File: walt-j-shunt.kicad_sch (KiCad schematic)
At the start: 39 parts, among them Q1 NMOS, Q2 PNP, Q3 PNP, U1 ${SIM.PARAMS}

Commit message: footprint placeholders
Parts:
- C4: footprint (none) -> Capacitor_THT:CP_Radial_D5.0mm_P2.00mm
- D5: footprint (none) -> Diode_SMD:D_0805_2012Metric
- D6, D7: footprint (none) -> Diode_SMD:D_SMC
- D8, D9: footprint (none) -> Package_TO_SOT_SMD:SOT-23-3
- Q1: footprint (none) -> Package_TO_SOT_THT:TO-3P-3_Horizontal_TabDown
- U1: footprint (none) -> Package_SO:SOIC-8-1EP_3.9x4.9mm_P1.27mm_EP2.41x3.3mm
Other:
- moved on the sheet: D8, R11, R12
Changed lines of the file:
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@@
 	)
 	(junction
-		(at 213.36 93.98)
+		(at 226.06 86.36)
 		(diameter 0)
 		(color 0 0 0 0)
 	)
 	(junction
-		(at 226.06 86.36)
+		(at 127 86.36)
 		(diameter 0)
 		(color 0 0 0 0)
 	)
 	(junction
-		(at 127 86.36)
+		(at 213.36 95.25)
 		(diameter 0)
 		(color 0 0 0 0)
@@
 	(wire
 		(pts
-			(xy 213.36 93.98) (xy 213.36 95.25)
-		)
-		(stroke
-			(width 0)
-			(type default)
-		)
-	)
-	(wire
-		(pts
-			(xy 219.71 93.98) (xy 220.98 93.98)
+			(xy 219.71 95.25) (xy 220.98 95.25)
 		)
 		(stroke
@@
 	(wire
 		(pts
-			(xy 220.98 93.98) (xy 220.98 86.36)
+			(xy 220.98 95.25) (xy 220.98 86.36)
 		)
 		(stroke
@@
 	(wire
 		(pts
-			(xy 213.36 92.71) (xy 213.36 93.98)
-		)
-		(stroke
-			(width 0)
-			(type default)
-		)
-	)
-	(wire
-		(pts
 			(xy 180.34 106.68) (xy 181.61 106.68)
 		)
@@
 	(wire
 		(pts
-			(xy 207.01 93.98) (xy 207.01 99.06)
+			(xy 207.01 95.25) (xy 207.01 99.06)
 		)
 		(stroke
@@
 	(wire
 		(pts
-			(xy 213.36 93.98) (xy 214.63 93.98)
+			(xy 213.36 95.25) (xy 214.63 95.25)
 		)
 		(stroke
@@
 	(wire
 		(pts
-			(xy 213.36 102.87) (xy 213.36 105.41)
+			(xy 213.36 95.25) (xy 213.36 93.98)
+		)
+		(stroke
+			(width 0)
+			(type default)
+		)
+	)
+	(wire
+		(pts
+			(xy 213.36 104.14) (xy 213.36 105.41)
 		)
 		(stroke
@@
 	(wire
 		(pts
+			(xy 213.36 95.25) (xy 213.36 96.52)
+		)
+		(stroke
+			(width 0)
+			(type default)
+		)
+	)
+	(wire
+		(pts
 			(xy 83.82 86.36) (xy 88.9 86.36)
 		)
@@
 	(wire
 		(pts
-			(xy 212.09 93.98) (xy 213.36 93.98)
+			(xy 212.09 95.25) (xy 213.36 95.25)
 		)
 		(stroke
@@
 	(global_label "vref"
 		(shape input)
-		(at 213.36 92.71 90)
+		(at 213.36 93.98 90)
 		(fields_autoplaced yes)
 		(effects
@@
 		)
 		(property "Intersheetrefs" "${INTERSHEET_REFS}"
-			(at 213.36 86.1567 90)
+			(at 213.36 87.4267 90)
 			(effects
 				(font
@@
 	(symbol
 		(lib_id "Device:R_Small")
-		(at 209.55 93.98 270)
+		(at 209.55 95.25 270)
 		(unit 1)
 		(exclude_from_sim no)
@@
 		(fields_autoplaced yes)
 		(property "Reference" "R11"
-			(at 209.55 88.9 90)
+			(at 209.55 90.17 90)
 			(effects
 				(font
@@
 		)
 		(property "Value" "1k"
-			(at 209.55 91.44 90)
+			(at 209.55 92.71 90)
 			(effects
 				(font
@@
 		)
 		(property "Footprint" "Resistor_SMD:R_1206_3216Metric"
-			(at 209.55 93.98 0)
+			(at 209.55 95.25 0)
 			(effects
 				(font
@@
 		)
 		(property "Datasheet" "~"
-			(at 209.55 93.98 0)
+			(at 209.55 95.25 0)
 			(effects
 				(font
@@
 		)
 		(property "Description" "Resistor, small symbol"
-			(at 209.55 93.98 0)
+			(at 209.55 95.25 0)
 			(effects
 				(font
@@
 			)
 		)
-		(property "Footprint" ""
+		(property "Footprint" "Diode_SMD:D_SMC"
 			(at 194.31 102.87 0)
 			(effects
@@
 			)
 		)
-		(property "Footprint" ""
+		(property "Footprint" "Diode_SMD:D_SMC"
 			(at 187.96 102.87 0)
 			(effects
@@
 			)
 		)
-		(property "Footprint" ""
+		(property "Footprint" "Diode_SMD:D_0805_2012Metric"
 			(at 153.67 101.6 0)
 			(effects
@@
 			)
 		)
-		(property "Footprint" ""
+		(property "Footprint" "Package_TO_SOT_THT:TO-3P-3_Horizontal_TabDown"
 			(at 111.76 83.82 0)
 			(effects
@@
 			)
 		)
-		(property "Footprint" ""
+		(property "Footprint" "Package_TO_SOT_SMD:SOT-23-3"
 			(at 213.36 109.22 0)
 			(effects
@@
 	(symbol
 		(lib_id "Device:D_Zener")
-		(at 213.36 99.06 90)
+		(at 213.36 100.33 90)
 		(unit 1)
 		(exclude_from_sim no)
@@
 		(fields_autoplaced yes)
 		(property "Reference" "D8"
-			(at 215.9 97.7899 90)
+			(at 215.9 99.0599 90)
 			(effects
 				(font
@@
 		)
 		(property "Value" "D_Zener"
-			(at 215.9 100.3299 90)
+			(at 215.9 101.5999 90)
 			(effects
 				(font
@@
 			)
 		)
-		(property "Footprint" ""
-			(at 213.36 99.06 0)
+		(property "Footprint" "Package_TO_SOT_SMD:SOT-23-3"
+			(at 213.36 100.33 0)
 			(effects
 				(font
@@
 		)
 		(property "Datasheet" "~"
-			(at 213.36 99.06 0)
+			(at 213.36 100.33 0)
 			(effects
 				(font
@@
 		)
 		(property "Description" "Zener diode"
-			(at 213.36 99.06 0)
+			(at 213.36 100.33 0)
 			(effects
 				(font
@@
 		)
 		(property "Sim.Library" "/Users/cibo/Documents/spice/d.lib"
-			(at 213.36 99.06 0)
+			(at 213.36 100.33 0)
 			(effects
 				(font
@@
 		)
 		(property "Sim.Name" "BZX84C6V2L"
-			(at 213.36 99.06 0)
+			(at 213.36 100.33 0)
 			(effects
 				(font
@@
 		)
 		(property "Sim.Device" "D"
-			(at 213.36 99.06 0)
+			(at 213.36 100.33 0)
 			(effects
 				(font
@@
 		)
 		(property "Sim.Pins" "1=K 2=A"
-			(at 213.36 99.06 0)
+			(at 213.36 100.33 0)
 			(effects
 				(font
@@
 			)
 		)
-		(property "Footprint" ""
+		(property "Footprint" "Capacitor_THT:CP_Radial_D5.0mm_P2.00mm"
 			(at 161.29 110.49 0)
 			(effects
@@
 	(symbol
 		(lib_id "Device:R_Small")
-		(at 217.17 93.98 270)
+		(at 217.17 95.25 270)
 		(unit 1)
 		(exclude_from_sim no)
@@
 		(fields_autoplaced yes)
 		(property "Reference" "R12"
-			(at 217.17 88.9 90)
+			(at 217.17 90.17 90)
 			(effects
 				(font
@@
 		)
 		(property "Value" "1.82k"
-			(at 217.17 91.44 90)
+			(at 217.17 92.71 90)
 			(effects
 				(font
@@
 		)
 		(property "Footprint" "Resistor_SMD:R_1206_3216Metric"
-			(at 217.17 93.98 0)
+			(at 217.17 95.25 0)
 			(effects
 				(font
@@
 		)
 		(property "Datasheet" "~"
-			(at 217.17 93.98 0)
+			(at 217.17 95.25 0)
 			(effects
 				(font
@@
 		)
 		(property "Description" "Resistor, small symbol"
-			(at 217.17 93.98 0)
+			(at 217.17 95.25 0)
 			(effects
 				(font
@@
 			)
 		)
-		(property "Footprint" ""
+		(property "Footprint" "Package_SO:SOIC-8-1EP_3.9x4.9mm_P1.27mm_EP2.41x3.3mm"
 			(at 166.37 101.6 0)
 			(effects

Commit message: basic layout positive
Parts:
- removed U1: ${SIM.PARAMS}, Package_SO:SOIC-8-1EP_3.9x4.9mm_P1.27mm_EP2.41x3.3mm, symbol Simulation_SPICE:OPAMP
- removed V1: VSIN, Samacsys:395443002, symbol Simulation_SPICE:VSIN
- added U1: AD817, Package_SO:SOIC-8_3.9x4.9mm_P1.27mm, symbol Amplifier_Operational:AD817
- added V1: VPULSE, Samacsys:395443002, symbol Simulation_SPICE:VPULSE
- C1, C2: footprint Capacitor_THT:CP_Radial_D18.0mm_P7.50mm -> Capacitor_THT:CP_Radial_D12.5mm_P5.00mm
- C3: footprint Capacitor_THT:CP_Radial_D18.0mm_P7.50mm -> Samacsys:B32529C105J
- C4: footprint Capacitor_THT:CP_Radial_D5.0mm_P2.00mm -> Capacitor_SMD:C_0805_2012Metric
- D1, D2, D3, D4: footprint Diode_SMD:D_SMC -> Diode_SMD:D_SOD-123
- D6, D7: footprint Diode_SMD:D_SMC -> Diode_SMD:D_SOD-123F
- Q1: footprint Package_TO_SOT_THT:TO-3P-3_Horizontal_TabDown -> Package_TO_SOT_THT:TO-220-3_Horizontal_TabDown
- Q2: footprint Package_TO_SOT_THT:TO-3P-3_Horizontal_TabDown -> Package_TO_SOT_SMD:TO-252-2
- Q3: footprint Package_TO_SOT_THT:TO-3P-3_Horizontal_TabDown -> Package_TO_SOT_SMD:SOT-23-3
- R10, R9: footprint Resistor_SMD:R_1206_3216Metric -> Resistor_SMD:R_MELF_MMB-0207
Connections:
- net GND: now also U1.4 (V-)
- net ac: now also V1.1
- net out: now also U1.7 (V+)
- net pre-cur: now reaches C3.1, Q1.1 (D), R2.1
- net at D1.2 (A), D2.1 (K): now also V1.2
- net at C6.1, D6.2 (A), D7.1 (K)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: now also U1.3 (+)
- net at C4.2, D5.1 (K): now also U1.6
- net at C4.1, R8.2: now also U1.2 (-)
- no-connect marks 0 -> 2
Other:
- moved on the sheet: D1, D3

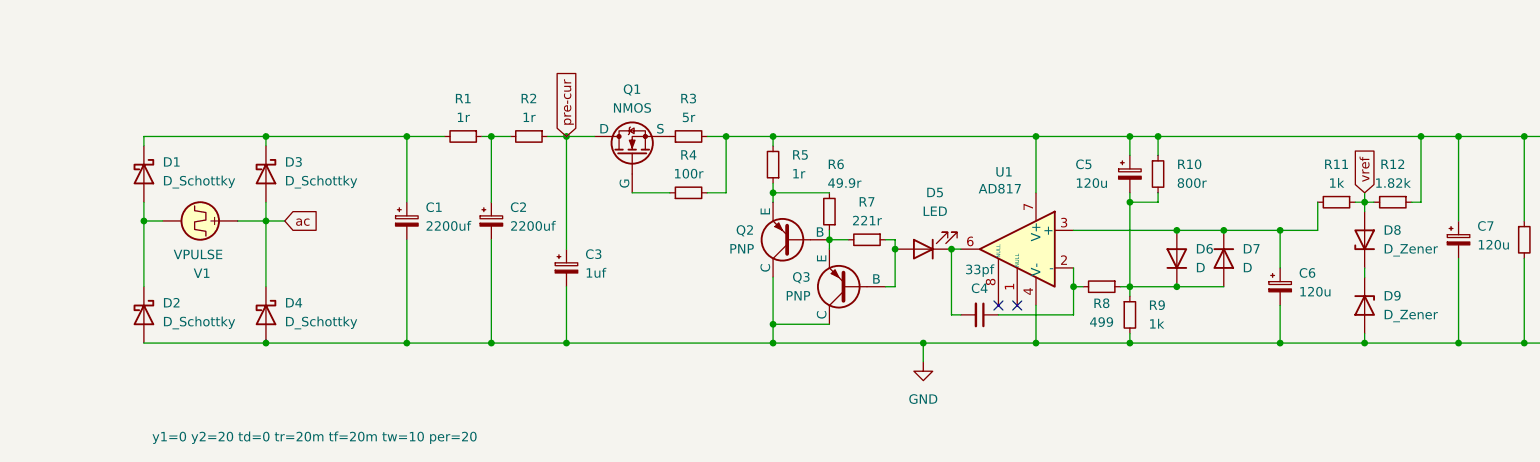
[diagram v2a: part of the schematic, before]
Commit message: plus only, cap and rectififer on board
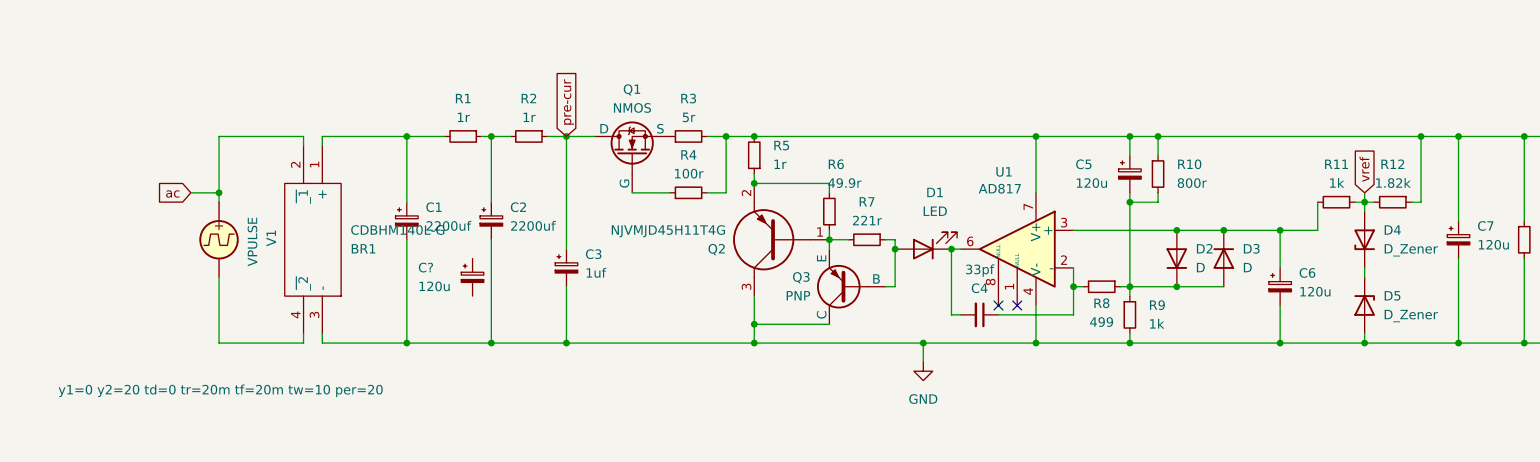
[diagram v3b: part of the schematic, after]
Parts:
- removed D1, D2, D3, D4: D_Schottky, Diode_SMD:D_SOD-123, symbol Device:D_Schottky
- removed Q2: PNP, Package_TO_SOT_SMD:TO-252-2, symbol Simulation_SPICE:PNP
- added BR1: CDBHM140L-G, Samacsys:CDBHM140LG, symbol Samacsys:CDBHM140L-G
- added C?: 120u, Capacitor_THT:CP_Radial_D5.0mm_P2.00mm, symbol Device:C_Polarized_Small
- added Q2: NJVMJD45H11T4G, Samacsys:DPAK_(SINGLE-GAUGE)_TO-252(369C)_ISSUE_F, symbol Samacsys:NJVMJD45H11T4G
- R13: footprint Resistor_SMD:R_2512_6332Metric -> Resistor_SMD:R_1206_3216Metric
- renumbered D5 to D1, D6 to D2, D7 to D3, D8 to D4, D9 to D5
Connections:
- net GND: now also BR1.3 (-), Q2.3
- net ac: now also BR1.2 (~{_1})
- net at Q3.3 (E), R6.1, R7.2: now also Q2.1
- net at R5.1, R6.2: now also Q2.2
- net at V1.2: now also BR1.4 (~{_2})
- net at C1.1, R1.2: now also BR1.1 (+)
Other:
- moved on the sheet: R5, V1

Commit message: working in subsheet
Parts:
- removed BR1: CDBHM140L-G, Samacsys:CDBHM140LG, symbol Samacsys:CDBHM140L-G
- removed C1, C2: 2200uf, Capacitor_THT:CP_Radial_D12.5mm_P5.00mm, symbol Device:C_Polarized_Small
- removed R1: 1r, Resistor_SMD:R_1206_3216Metric, symbol Device:R_Small
- removed R13: 1k, Resistor_SMD:R_1206_3216Metric, symbol Device:R_Small
- removed V1: VPULSE, Samacsys:395443002, symbol Simulation_SPICE:VPULSE
- added V1: VSIN, Samacsys:395443002, symbol Simulation_SPICE:VSIN
- D4, D5: footprint Package_TO_SOT_SMD:SOT-23-3 -> Diode_SMD:D_MiniMELF
- gave numbers to parts that had none: 1
- renumbered C3 to C2, C4 to C3, C5 to C4, C6 to C5, C7 to C6, R2 to R1, R11 to R10, R12 to R11, R3 to R2, R4 to R3, R5 to R4, R6 to R5, R7 to R6, R8 to R7, R9 to R8, R10 to R9
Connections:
- net GND: now also C1.2, V1.2
- net bank-plus: now reaches R1.2
- net bank-plus: now also C1.1, V1.1
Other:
- added sheet reg (reg.kicad_sch)
- moved on the sheet: C1, C2, I1, R1

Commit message: bipolar. untested
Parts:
- removed C3: 33pf, Capacitor_SMD:C_0805_2012Metric, symbol Device:C_Small
- removed C4, C5, C6: 120u, Capacitor_THT:CP_Radial_D5.0mm_P2.00mm, symbol Device:C_Polarized_Small
- removed D1: LED, Diode_SMD:D_0805_2012Metric, symbol Device:LED
- removed D2, D3: D, Diode_SMD:D_SOD-123F, symbol Device:D
- removed D4, D5: D_Zener, Diode_SMD:D_MiniMELF, symbol Device:D_Zener
- removed Q1: NMOS, Package_TO_SOT_THT:TO-220-3_Horizontal_TabDown, symbol Simulation_SPICE:NMOS
- removed Q2: NJVMJD45H11T4G, Samacsys:DPAK_(SINGLE-GAUGE)_TO-252(369C)_ISSUE_F, symbol Samacsys:NJVMJD45H11T4G
- removed Q3: PNP, Package_TO_SOT_SMD:SOT-23-3, symbol Simulation_SPICE:PNP
- removed R10: 1k, Resistor_SMD:R_1206_3216Metric, symbol Device:R_Small
- removed R11: 1.82k, Resistor_SMD:R_1206_3216Metric, symbol Device:R_Small
- removed R2: 5r, Resistor_SMD:R_1206_3216Metric, symbol Device:R_Small
- removed R3: 100r, Resistor_SMD:R_1206_3216Metric, symbol Device:R_Small
- removed R4: 1r, Resistor_SMD:R_1206_3216Metric, symbol Device:R_Small
- removed R5: 49.9r, Resistor_SMD:R_1206_3216Metric, symbol Device:R_Small
- removed R6: 221r, Resistor_SMD:R_1206_3216Metric, symbol Device:R_Small
- removed R7: 499, Resistor_SMD:R_1206_3216Metric, symbol Device:R_Small
- removed R8: 1k, Resistor_SMD:R_MELF_MMB-0207, symbol Device:R_Small
- removed R9: 800r, Resistor_SMD:R_MELF_MMB-0207, symbol Device:R_Small
- removed U1: AD817, Package_SO:SOIC-8_3.9x4.9mm_P1.27mm, symbol Amplifier_Operational:AD817
- added C7: 120u, Capacitor_THT:CP_Radial_D5.0mm_P2.00mm, symbol Device:C_Polarized_Small
- added C8: 1uf, Samacsys:B32529C105J, symbol Device:C_Polarized_Small
- added I2: 20ma, Samacsys:395443002, symbol Simulation_SPICE:IDC
- added R12: 1r, Resistor_SMD:R_1206_3216Metric, symbol Device:R_Small
- added V2: VSIN, Samacsys:395443002, symbol Simulation_SPICE:VSIN
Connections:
- net GND: now also C7.1, C8.1, I2.1, V2.1
- net out renamed pos_reg_out
- new net: C7.2, R12.2, V2.2
- new net current_source1/plus: C8.2, R12.1
- new net neg_reg_out: I2.2
- no-connect marks 2 -> 0
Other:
- added sheet current_source (current_source.kicad_sch)
- added sheet current_source1 (current_source.kicad_sch)
- added sheet reg1 (reg.kicad_sch)
- sheet reg ports: added minus, plus; removed none
- moved on the sheet: C1, I1, R1

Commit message: pretty neat neg needs testing
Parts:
- added J1: Screw_Terminal_01x03, TerminalBlock_Altech:Altech_AK100_1x03_P5.00mm, symbol Connector:Screw_Terminal_01x03
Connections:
- net GND: now also J1.2 (Pin_2)
- net neg_reg_out: now also J1.3 (Pin_3)
- net pos_reg_out: now also J1.1 (Pin_1)
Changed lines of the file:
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@@
 	(paper "A4")
 	(junction
+		(at 170.18 153.67)
+		(diameter 0)
+		(color 0 0 0 0)
+	)
+	(junction
 		(at 158.75 95.25)
 		(diameter 0)
@@
 	)
 	(junction
+		(at 170.18 95.25)
+		(diameter 0)
+		(color 0 0 0 0)
+	)
+	(junction
 		(at 97.79 114.3)
 		(diameter 0)
@@
 	)
 	(junction
+		(at 157.48 153.67)
+		(diameter 0)
+		(color 0 0 0 0)
+	)
+	(junction
 		(at 130.81 114.3)
 		(diameter 0)
@@
 	)
 	(junction
+		(at 138.43 114.3)
+		(diameter 0)
+		(color 0 0 0 0)
+	)
+	(junction
 		(at 96.52 153.67)
 		(diameter 0)
@@
 	(wire
 		(pts
+			(xy 171.45 127) (xy 170.18 127)
+		)
+		(stroke
+			(width 0)
+			(type default)
+		)
+	)
+	(wire
+		(pts
 			(xy 130.81 134.62) (xy 143.51 134.62)
 		)
@@
 	(wire
 		(pts
+			(xy 171.45 124.46) (xy 138.43 124.46)
+		)
+		(stroke
+			(width 0)
+			(type default)
+		)
+	)
+	(wire
+		(pts
 			(xy 87.63 114.3) (xy 97.79 114.3)
 		)
@@
 	(wire
 		(pts
-			(xy 142.24 114.3) (xy 130.81 114.3)
+			(xy 157.48 153.67) (xy 157.48 144.78)
+		)
+		(stroke
+			(width 0)
+			(type default)
+		)
+	)
+	(wire
+		(pts
+			(xy 157.48 153.67) (xy 170.18 153.67)
+		)
+		(stroke
+			(width 0)
+			(type default)
+		)
+	)
+	(wire
+		(pts
+			(xy 142.24 114.3) (xy 138.43 114.3)
 		)
 		(stroke
@@
 	(wire
 		(pts
+			(xy 170.18 127) (xy 170.18 153.67)
+		)
+		(stroke
+			(width 0)
+			(type default)
+		)
+	)
+	(wire
+		(pts
 			(xy 86.36 134.62) (xy 96.52 134.62)
 		)
@@
 	(wire
 		(pts
-			(xy 157.48 144.78) (xy 157.48 153.67)
+			(xy 138.43 114.3) (xy 130.81 114.3)
 		)
 		(stroke
@@
 	(wire
 		(pts
+			(xy 138.43 124.46) (xy 138.43 114.3)
+		)
+		(stroke
+			(width 0)
+			(type default)
+		)
+	)
+	(wire
+		(pts
 			(xy 96.52 134.62) (xy 106.68 134.62)
 		)
@@
 	(wire
 		(pts
+			(xy 173.99 95.25) (xy 170.18 95.25)
+		)
+		(stroke
+			(width 0)
+			(type default)
+		)
+	)
+	(wire
+		(pts
 			(xy 97.79 104.14) (xy 97.79 114.3)
 		)
@@
 	(wire
 		(pts
-			(xy 158.75 95.25) (xy 162.56 95.25)
+			(xy 170.18 121.92) (xy 170.18 95.25)
+		)
+		(stroke
+			(width 0)
+			(type default)
+		)
+	)
+	(wire
+		(pts
+			(xy 171.45 121.92) (xy 170.18 121.92)
+		)
+		(stroke
+			(width 0)
+			(type default)
+		)
+	)
+	(wire
+		(pts
+			(xy 158.75 95.25) (xy 170.18 95.25)
 		)
 		(stroke
@@
 		(pts
 			(xy 86.36 134.62) (xy 86.36 142.24)
+		)
+		(stroke
+			(width 0)
+			(type default)
+		)
+	)
+	(wire
+		(pts
+			(xy 170.18 153.67) (xy 176.53 153.67)
 		)
 		(stroke
@@
 	(global_label "pos_reg_out"
 		(shape input)
-		(at 162.56 95.25 0)
+		(at 173.99 95.25 0)
 		(fields_autoplaced yes)
 		(effects
@@
 		)
 		(property "Intersheetrefs" "${INTERSHEET_REFS}"
-			(at 176.854 95.25 0)
+			(at 188.284 95.25 0)
 			(effects
 				(font
@@
 	(global_label "neg_reg_out"
 		(shape input)
-		(at 157.48 153.67 0)
+		(at 176.53 153.67 0)
 		(fields_autoplaced yes)
 		(effects
@@
 		)
 		(property "Intersheetrefs" "${INTERSHEET_REFS}"
-			(at 171.8345 153.67 0)
+			(at 190.8845 153.67 0)
 			(effects
 				(font
@@
 		(exclude_from_sim no)
 		(in_bom yes)
-		(on_board yes)
+		(on_board no)
 		(dnp no)
 		(fields_autoplaced yes)
@@
 				(path "/c8b32050-fabe-49d4-b213-dd23b367e349"
 					(reference "C1")
+					(unit 1)
+				)
+			)
+		)
+	)
+	(symbol
+		(lib_id "Connector:Screw_Terminal_01x03")
+		(at 176.53 124.46 0)
+		(unit 1)
+		(exclude_from_sim no)
+		(in_bom yes)
+		(on_board yes)
+		(dnp no)
+		(fields_autoplaced yes)
+		(property "Reference" "J1"
+			(at 179.07 123.1899 0)
+			(effects
+				(font
+					(size 1.27 1.27)
+				)
+				(justify left)
+			)
+		)
+		(property "Value" "Screw_Terminal_01x03"
+			(at 179.07 125.7299 0)
+			(effects
+				(font
+					(size 1.27 1.27)
+				)
+				(justify left)
+			)
+		)
+		(property "Footprint" "TerminalBlock_Altech:Altech_AK100_1x03_P5.00mm"
+			(at 176.53 124.46 0)
+			(effects
+				(font
+					(size 1.27 1.27)
+				)
+				(hide yes)
+			)
+		)
+		(property "Datasheet" "~"
+			(at 176.53 124.46 0)
+			(effects
+				(font
+					(size 1.27 1.27)
+				)
+				(hide yes)
+			)
+		)
+		(property "Description" "Generic screw terminal, single row, 01x03, script generated (kicad-library-utils/schlib/autogen/connector/)"
+			(at 176.53 124.46 0)
+			(effects
+				(font
+					(size 1.27 1.27)
+				)
+				(hide yes)
+			)
+		)
+		(pin "2"
+		)
+		(pin "1"
+		)
+		(pin "3"
+		)
+		(instances
+			(project ""
+				(path "/c8b32050-fabe-49d4-b213-dd23b367e349"
+					(reference "J1")
 					(unit 1)
 				)
@@
 		(exclude_from_sim no)
 		(in_bom yes)
-		(on_board yes)
+		(on_board no)
 		(dnp no)
 		(fields_autoplaced yes)
